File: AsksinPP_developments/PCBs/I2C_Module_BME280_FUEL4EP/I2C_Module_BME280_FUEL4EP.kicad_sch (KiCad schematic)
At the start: 12 parts, among them J1 Conn_01x04, J2 Conn_01x04, U1 BME280

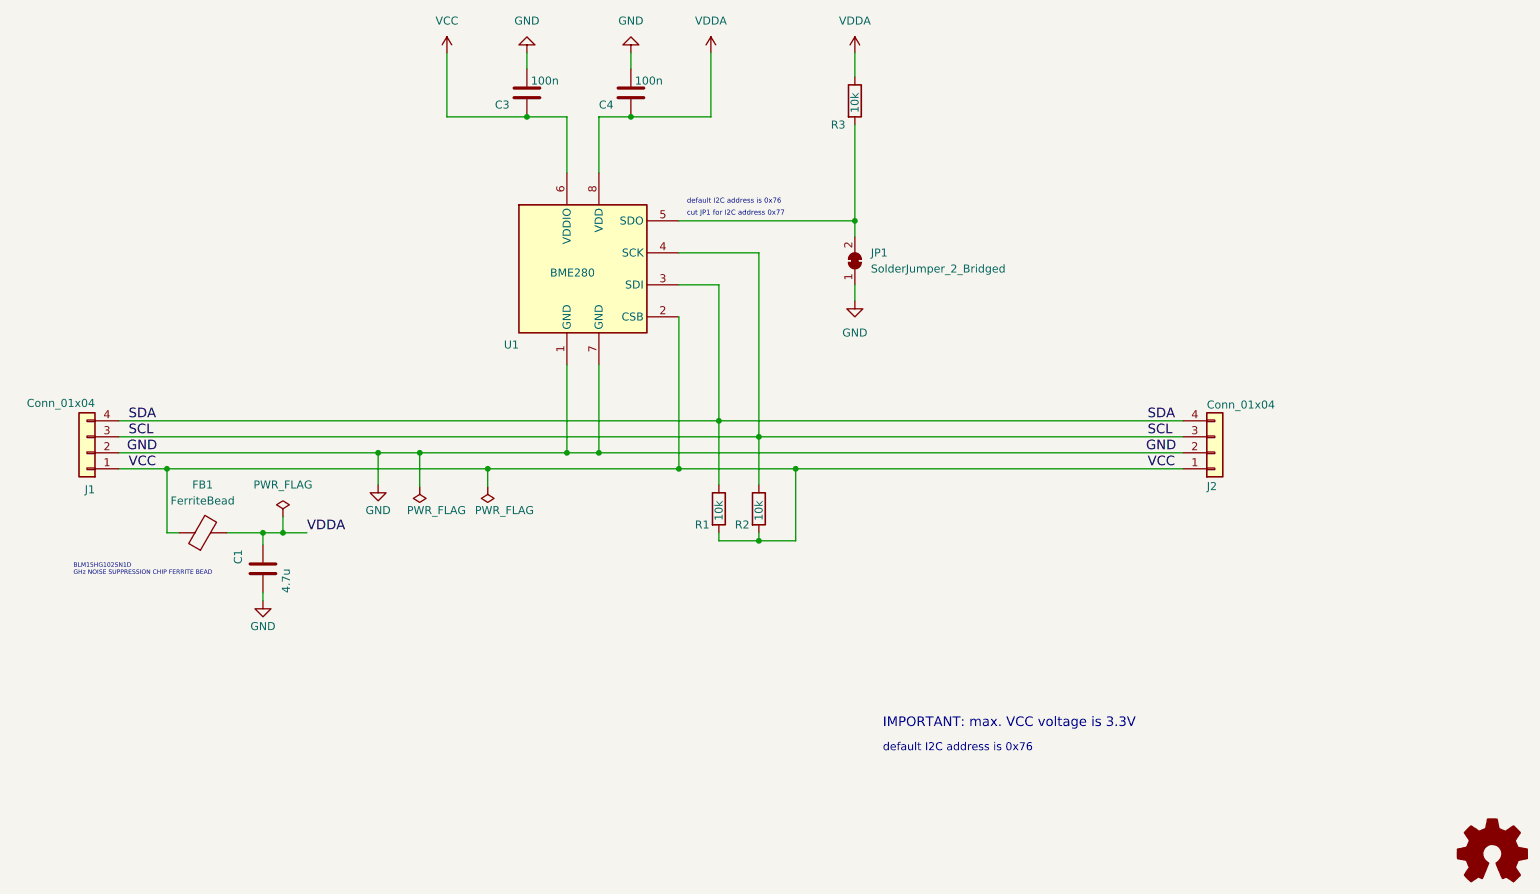
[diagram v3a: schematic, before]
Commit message: PCBs: upgrade some PCBs to KiCAD 7; fix of unnecessary leakage current of I2C address selector: I2C_Module_SHT85_BME280_FUEL4EP, I2C_Module_SHT45_BME280_small_FUEL4EP, I2C_Module_SHT45_BME280_FUEL4EP, I2C_Module_BME280_FUEL4EP, and I2C_Module_BME680_FUEL4EP
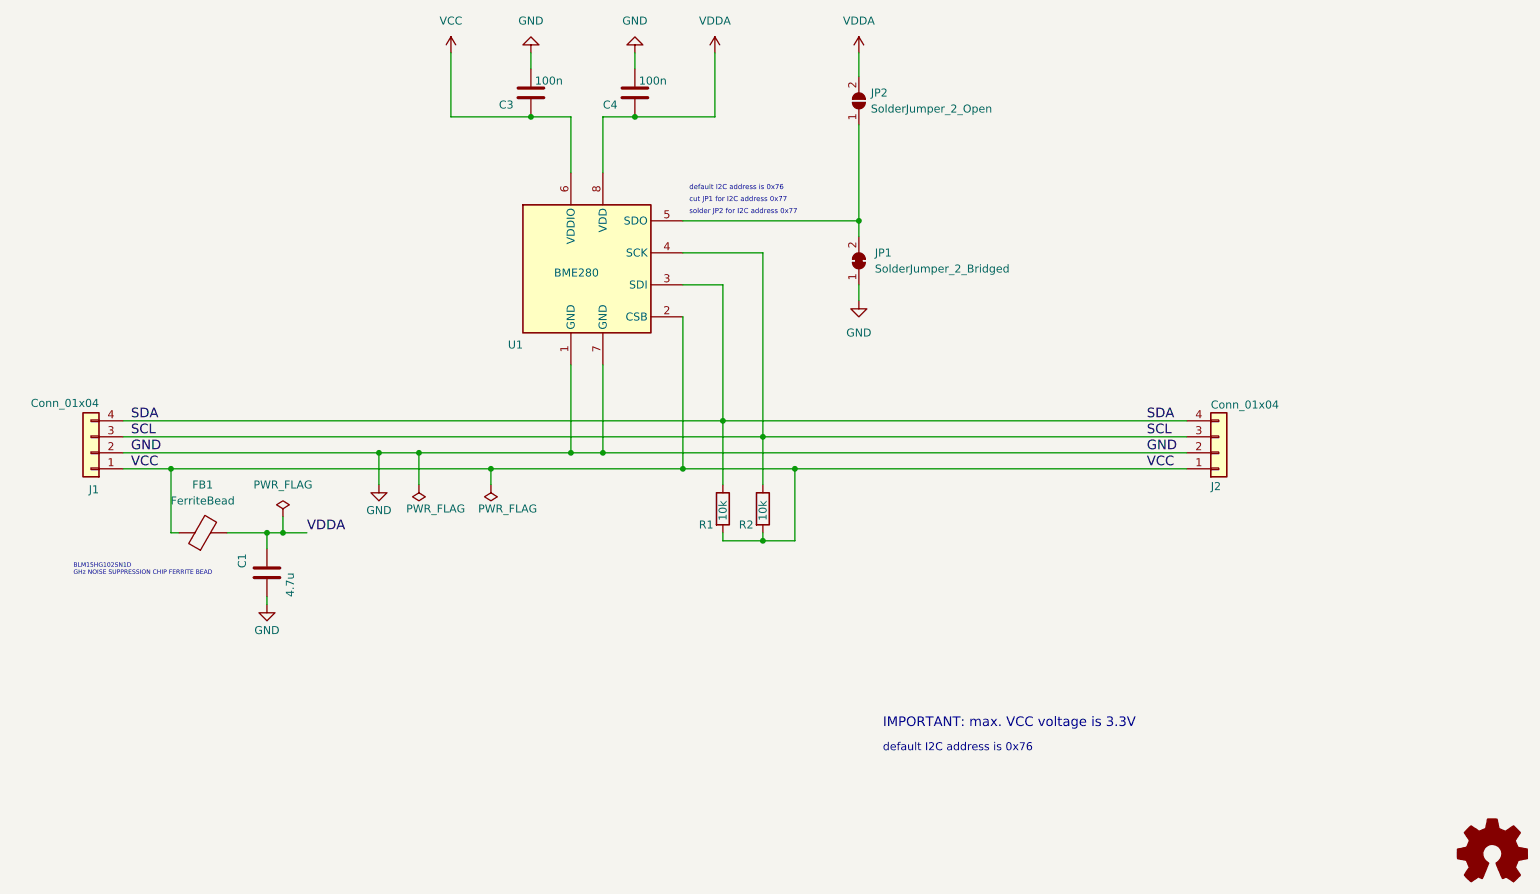
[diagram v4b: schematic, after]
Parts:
- removed R3: 10k, Resistor_SMD:R_0402_1005Metric, symbol Device:R
- added JP2: SolderJumper_2_Open, Jumper:SolderJumper-2_P1.3mm_Open_Pad1.0x1.5mm, symbol Jumper:SolderJumper_2_Open
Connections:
- net VDDA: now also JP2.2 (B)
- net at JP1.2 (B), U1.5 (SDO): now also JP2.1 (A)
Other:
- note added: "solder JP2 for I2C address 0x77"
- moved on the sheet: C1, C3, C4, J1, J2, JP1, R1, R2, U1

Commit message: PCBs/I2C_Module_SHT45_BME280_FUEL4EP und PCBs/I2C_Module_BME280_FUEL4EP: migration to KiCAD 8; fix of DRC rules for PCBs/I2C_Module_SHT45_BME280_FUEL4EP
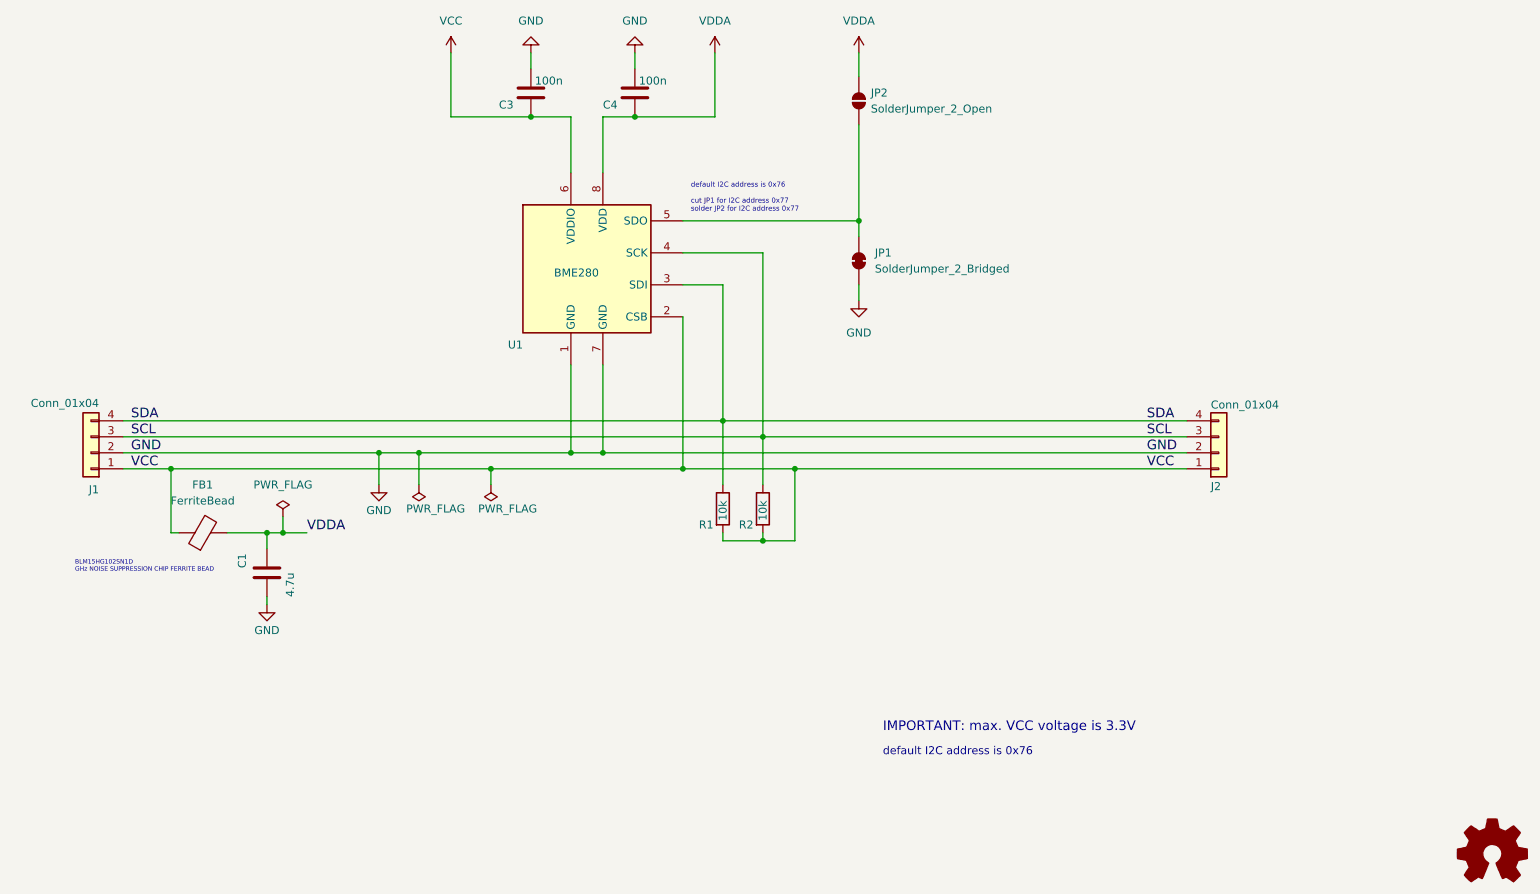
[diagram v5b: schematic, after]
